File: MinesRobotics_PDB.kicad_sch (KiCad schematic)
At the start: 5 parts, among them J1 Conn_01x02_Male

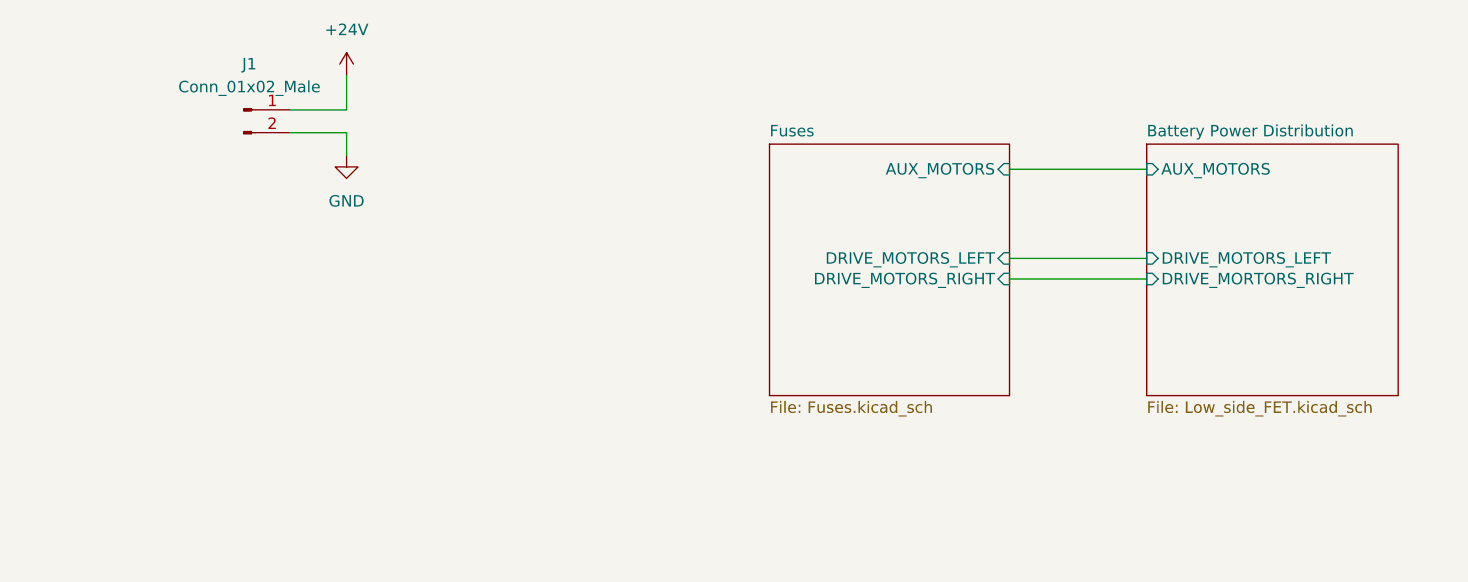
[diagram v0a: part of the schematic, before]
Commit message: Added 9V buck converter
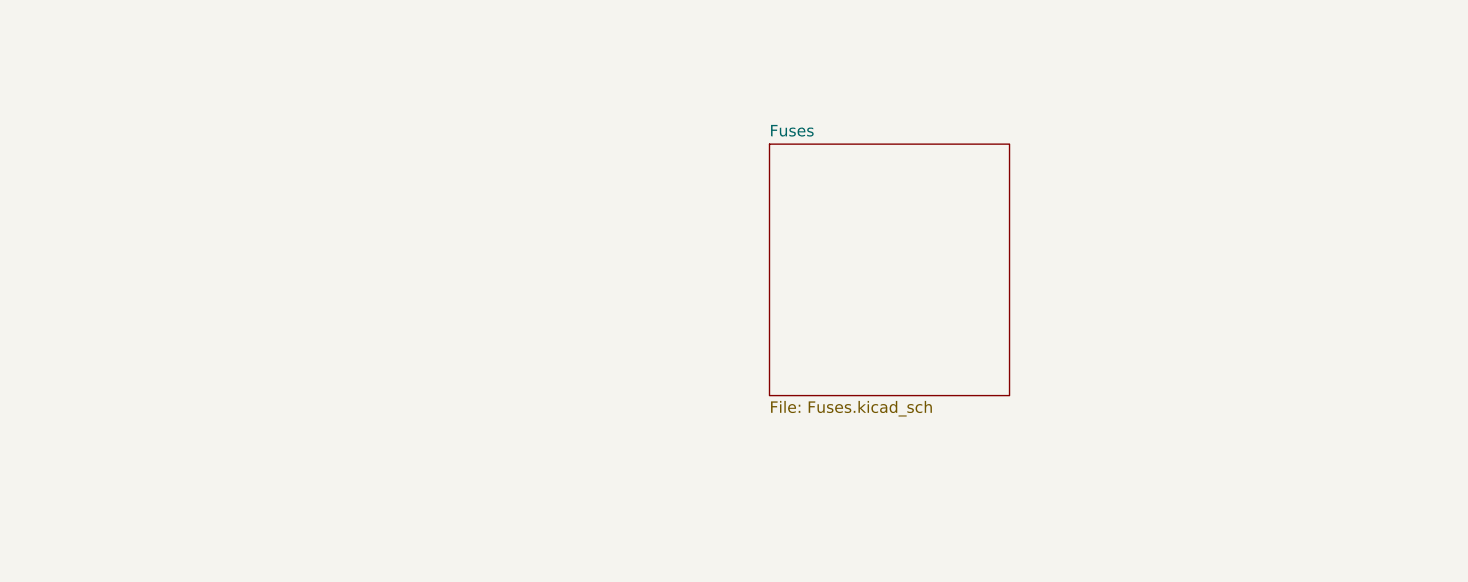
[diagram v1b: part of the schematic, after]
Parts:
- removed J1: Conn_01x02_Male, symbol Connector:Conn_01x02_Male
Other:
- removed sheet Battery Power Distribution
- sheet Fuses ports: added none; removed AUX_MOTORS, DRIVE_MOTORS_LEFT, DRIVE_MOTORS_RIGHT

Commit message: Cleaning up for prototype run
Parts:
- added H5, H6, H7: MountingHole_Pad, MountingHole:MountingHole_3.2mm_M3_DIN965_Pad, symbol Mechanical:MountingHole_Pad
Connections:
- net GND: now also H5.1, H6.1, H7.1
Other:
- sheet 5V Power renamed Buck converter
- moved on the sheet: H1, H2, H3, H4

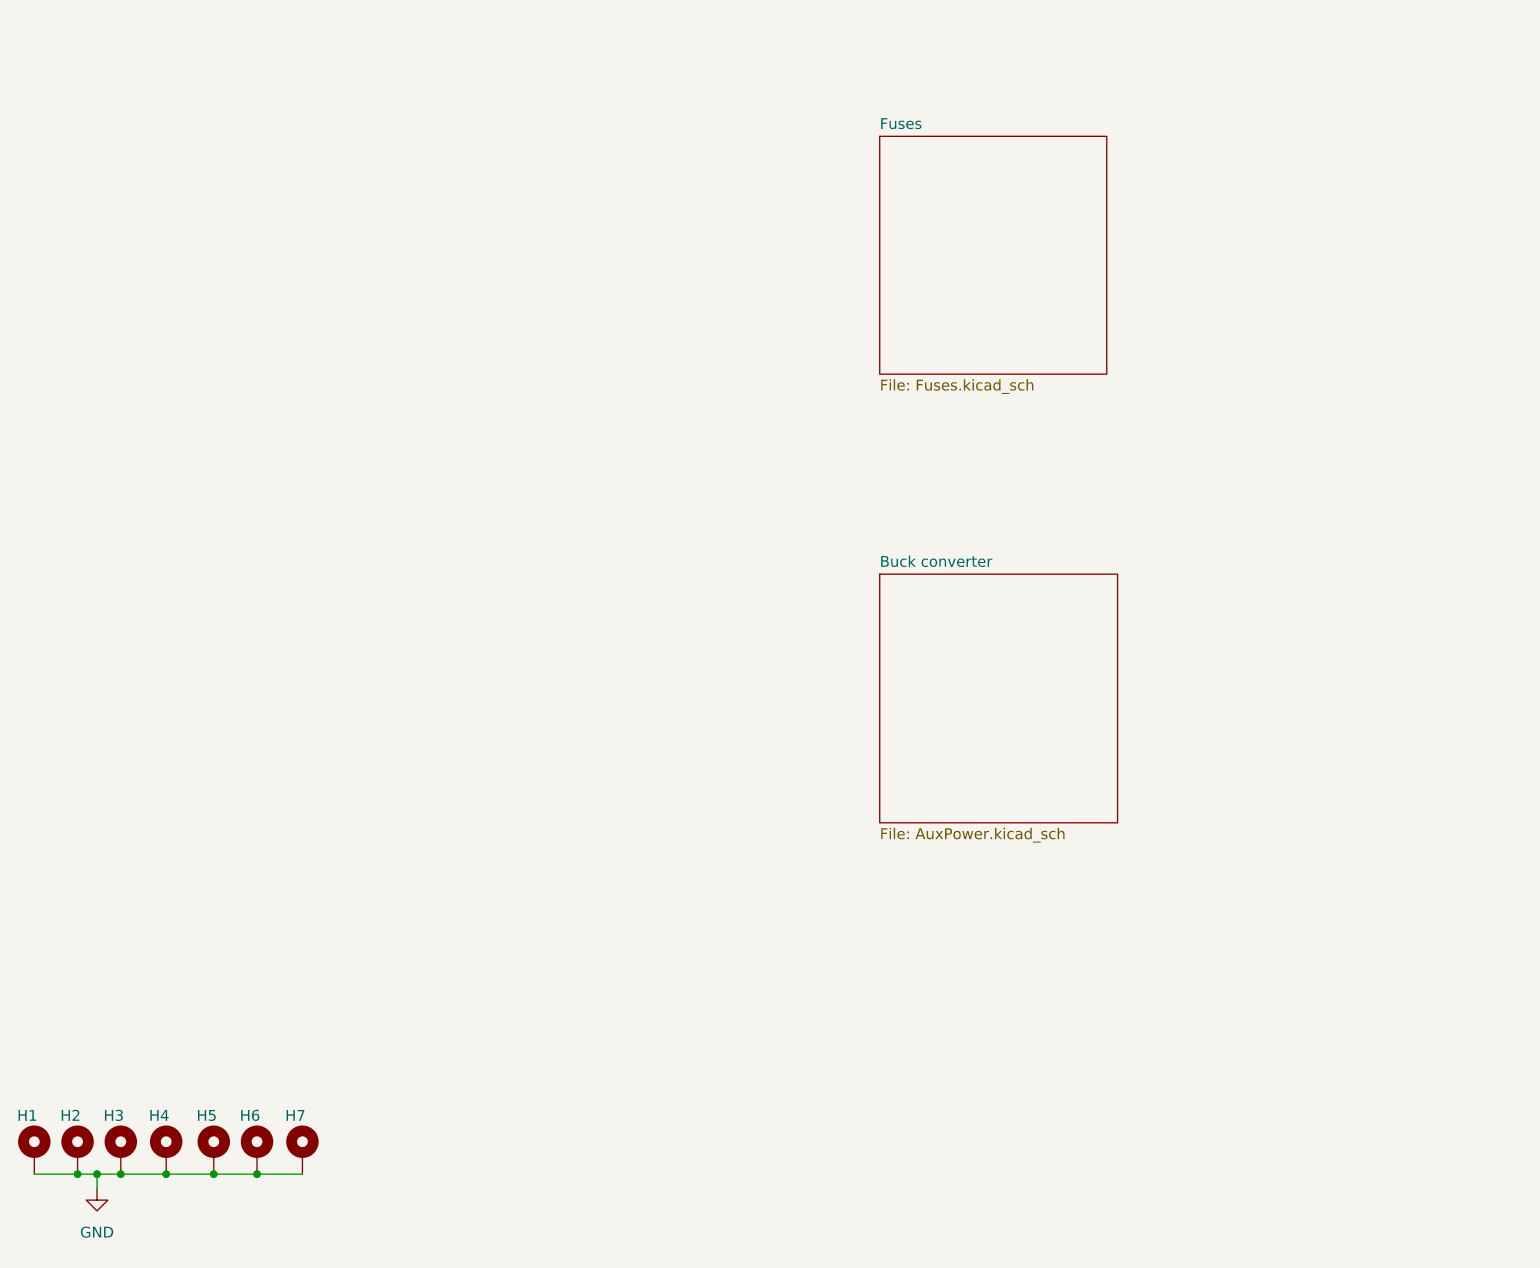
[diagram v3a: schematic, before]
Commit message: Added BOM and updated Cap footprint according to availability
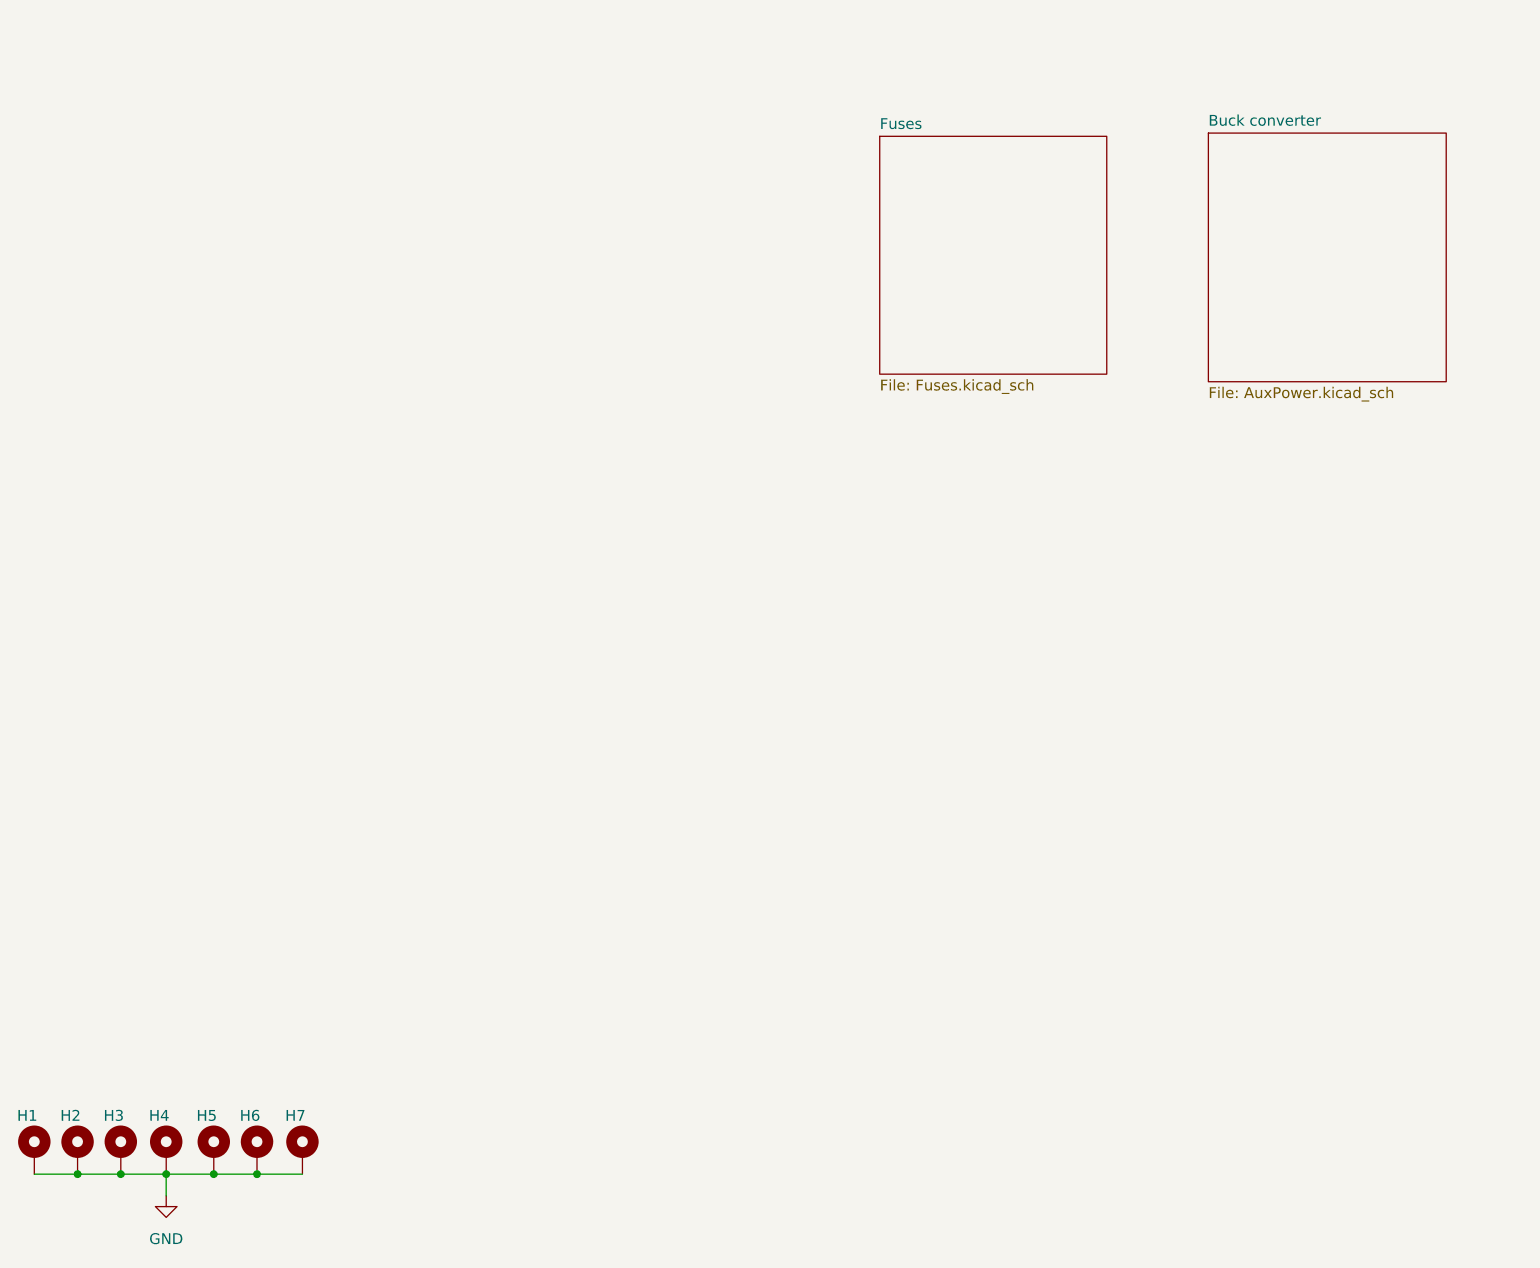
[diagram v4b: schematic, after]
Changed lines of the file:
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@@
   (junction (at 20.066 185.42) (diameter 0) (color 0 0 0 0)
   )
-  (junction (at 22.352 185.42) (diameter 0) (color 0 0 0 0)
-  )
   (junction (at 25.146 185.42) (diameter 0) (color 0 0 0 0)
   )
   (junction (at 36.068 185.42) (diameter 0) (color 0 0 0 0)
   )
-  (wire (pts (xy 25.146 185.42) (xy 22.352 185.42))
-    (stroke (width 0) (type default) (color 0 0 0 0))
-  )
   (wire (pts (xy 41.148 185.42) (xy 46.482 185.42))
     (stroke (width 0) (type default) (color 0 0 0 0))
   )
-  (wire (pts (xy 22.352 185.42) (xy 22.352 187.198))
-    (stroke (width 0) (type default) (color 0 0 0 0))
-  )
-  (wire (pts (xy 22.352 185.42) (xy 20.066 185.42))
+  (wire (pts (xy 30.48 185.42) (xy 30.48 187.96))
+    (stroke (width 0) (type default) (color 0 0 0 0))
+  )
+  (wire (pts (xy 25.146 185.42) (xy 20.066 185.42))
     (stroke (width 0) (type default) (color 0 0 0 0))
   )
@@
     (pin "1")
   )
-  (symbol (lib_id "power:GND") (at 22.352 187.198 0) (unit 1)
+  (symbol (lib_id "power:GND") (at 30.48 187.96 0) (unit 1)
     (in_bom yes) (on_board yes) (fields_autoplaced)
-    (property "Reference" "#PWR01" (id 0) (at 22.352 193.548 0)
-      (effects (font (size 1.27 1.27)) hide)
-    )
-    (property "Value" "GND" (id 1) (at 22.352 192.278 0))
-    (property "Footprint" "" (id 2) (at 22.352 187.198 0)
-      (effects (font (size 1.27 1.27)) hide)
-    )
-    (property "Datasheet" "" (id 3) (at 22.352 187.198 0)
+    (property "Reference" "#PWR01" (id 0) (at 30.48 194.31 0)
+      (effects (font (size 1.27 1.27)) hide)
+    )
+    (property "Value" "GND" (id 1) (at 30.48 193.04 0))
+    (property "Footprint" "" (id 2) (at 30.48 187.96 0)
+      (effects (font (size 1.27 1.27)) hide)
+    )
+    (property "Datasheet" "" (id 3) (at 30.48 187.96 0)
       (effects (font (size 1.27 1.27)) hide)
     )
@@
   )
   (sheet (at 114.3 63.5) (size 26.67 27.94) (fields_autoplaced)
-    (stroke (width 0.1524) (type solid) (color 0 0 0 0))
-    (fill (color 0 0 0 0.0000))
+    (stroke (width 0.1524) (type solid) (color 194 0 0 1))
+    (fill (color 0 194 194 1.0000))
     (property "Sheet name" "Fuses" (id 0) (at 114.3 62.7884 0)
       (effects (font (size 1.27 1.27)) (justify left bottom))
@@
     )
   )
-  (sheet (at 114.3 114.935) (size 27.94 29.21) (fields_autoplaced)
-    (stroke (width 0.1524) (type solid) (color 0 0 0 0))
-    (fill (color 0 0 0 0.0000))
-    (property "Sheet name" "Buck converter" (id 0) (at 114.3 114.2234 0)
+  (sheet (at 152.908 63.119) (size 27.94 29.21) (fields_autoplaced)
+    (stroke (width 0.1524) (type solid) (color 194 0 0 1))
+    (fill (color 0 194 194 1.0000))
+    (property "Sheet name" "Buck converter" (id 0) (at 152.908 62.4074 0)
       (effects (font (size 1.27 1.27)) (justify left bottom))
     )
-    (property "Sheet file" "AuxPower.kicad_sch" (id 1) (at 114.3 144.7296 0)
+    (property "Sheet file" "AuxPower.kicad_sch" (id 1) (at 152.908 92.9136 0)
       (effects (font (size 1.27 1.27)) (justify left top))
     )
@@
       (reference "#PWR0117") (unit 1) (value "+9V") (footprint "")
     )
-    (path "/6a43cbc3-957c-4b7d-9dbc-8c3175b73e7e/9b348643-535f-4024-a7d0-4b7309f7b221"
-      (reference "C1") (unit 1) (value "100u") (footprint "Capacitor_SMD:C_0603_1608Metric")
+    (path "/6a43cbc3-957c-4b7d-9dbc-8c3175b73e7e/d5f0102a-ccd2-481d-aac9-a500663069d8"
+      (reference "C1") (unit 1) (value "100u") (footprint "Capacitor_SMD:CP_Elec_10x10")
     )
     (path "/6a43cbc3-957c-4b7d-9dbc-8c3175b73e7e/ca9b4d23-33dc-44bf-bcd4-ceca80f4808b"
@@
     )
     (path "/6a43cbc3-957c-4b7d-9dbc-8c3175b73e7e/474561c1-26a1-4205-b0f8-f525b846a87d"
-      (reference "C3") (unit 1) (value "22u") (footprint "Capacitor_SMD:C_0603_1608Metric")
+      (reference "C3") (unit 1) (value "22u") (footprint "Capacitor_Tantalum_SMD:CP_EIA-7343-15_Kemet-W")
     )
     (path "/6a43cbc3-957c-4b7d-9dbc-8c3175b73e7e/4b164835-6c8b-4c95-af30-50c82dd25735"
